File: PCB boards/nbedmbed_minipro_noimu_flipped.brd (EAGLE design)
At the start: 63.5 x 47 mm, 16 parts

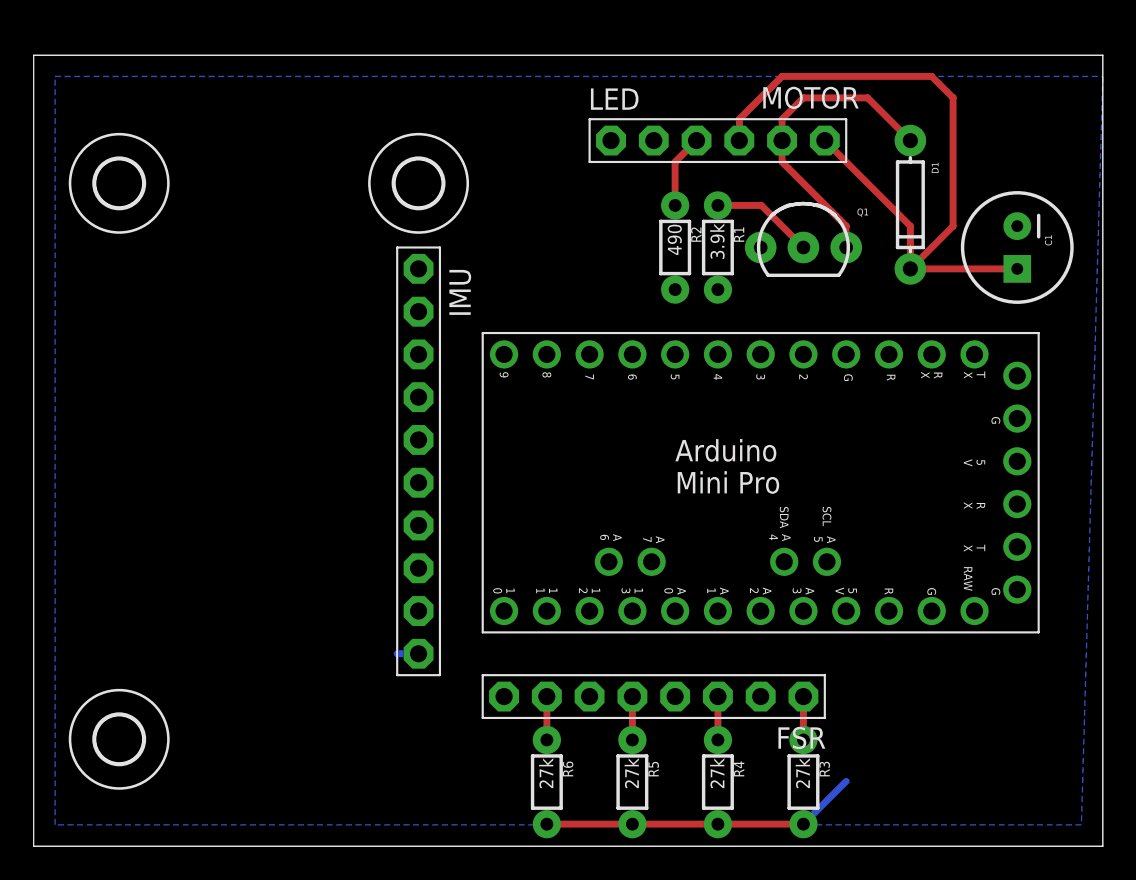
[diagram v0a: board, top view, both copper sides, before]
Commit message: updated arduino code
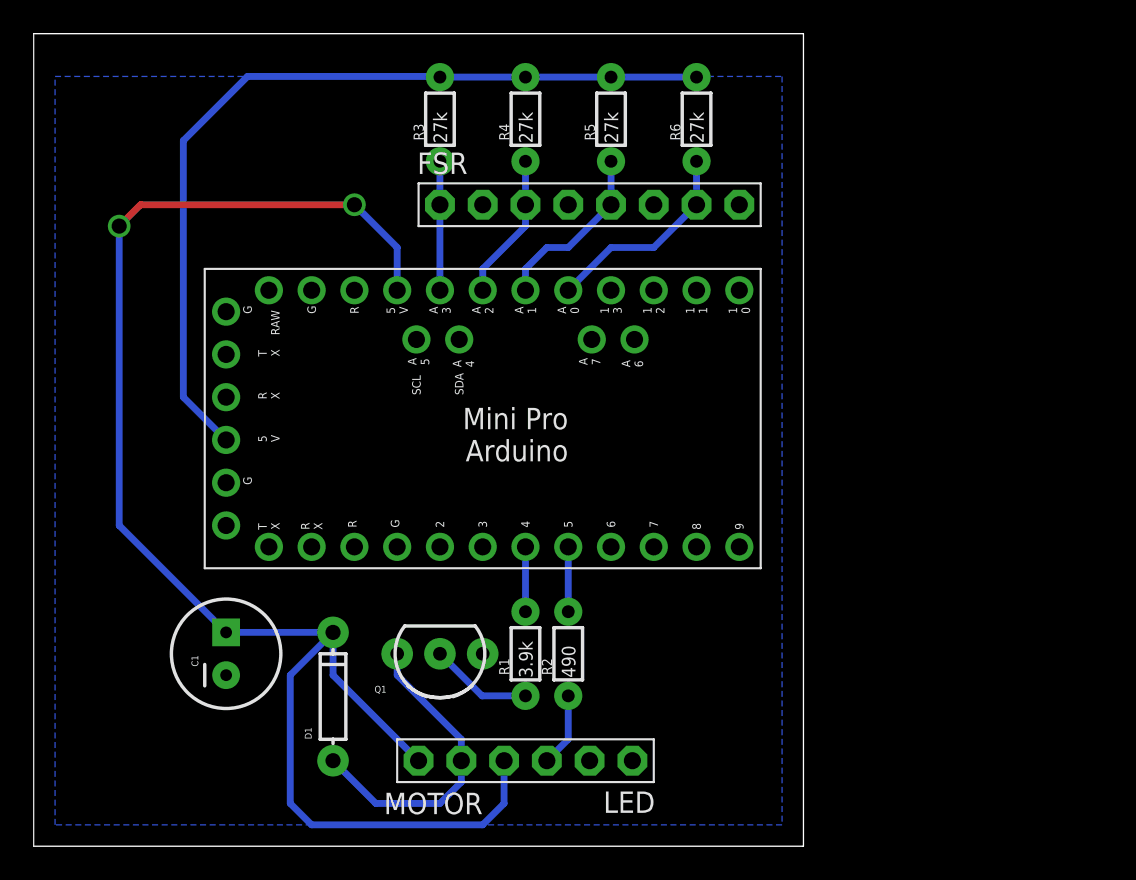
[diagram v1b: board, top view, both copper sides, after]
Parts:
- removed H1, H2, H3: MOUNT-HOLE2.8, holes:2,8
- removed IMU: 9D0F, adafruit:1X10-BIG
- moved C1 52.8 mm to (11.4, 11.4), turned to 90 degrees
- moved D1 45.0 mm to (17.8, 8.89), turned to 90 degrees
- moved R3 44.9 mm to (24.1, 43.2), turned to 90 degrees
- moved R4 41.0 mm to (29.2, 43.2), turned to 90 degrees
- moved R6 40.4 mm to (39.4, 43.2), turned to 90 degrees
- moved R5 39.4 mm to (34.3, 43.2), turned to 90 degrees
- moved LED 38.6 mm to (29.2, 5.08), turned to 180 degrees
- moved Q1 32.4 mm to (24.1, 11.4), turned to 180 degrees
- moved FSR 29.5 mm to (33.0, 38.1), turned to 0 degrees
- moved PCB2 27.2 mm to (43.2, 34.3), turned to 180 degrees
- moved R1 26.7 mm to (29.2, 11.4), turned to 90 degrees
- moved R2 25.0 mm to (31.8, 11.4), turned to 90 degrees
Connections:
- removed net N$10: IMU.6, PCB2.A4
- removed net N$11: IMU.7, PCB2.A5
- net FSR/IMU_5V: now also PCB2.5V.; no longer IMU.10, PCB2.5V
- net GND: no longer IMU.8, PCB2...GND
- net MOTOR/LED_5V: now also PCB2.5V; no longer PCB2.5V.
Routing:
- net MOTOR/LED_5V: track 42.8 -> 91.0 mm, vias 0 -> 2
- net FSR/IMU_5V: track 20.1 -> 50.9 mm
- net N$9: track 2.58 -> 12.3 mm
- net N$8: track 2.58 -> 10.5 mm
- net N$6: track 2.58 -> 8.71 mm
- net N$5: track 2.58 -> 7.66 mm
- net N$2: track 0.00 -> 3.85 mm
- net N$1: track 0.00 -> 3.85 mm
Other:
- board size 63.5 x 47 mm -> 45.7 x 48.3 mm
